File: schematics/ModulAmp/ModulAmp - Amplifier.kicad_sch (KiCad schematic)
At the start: 0 parts

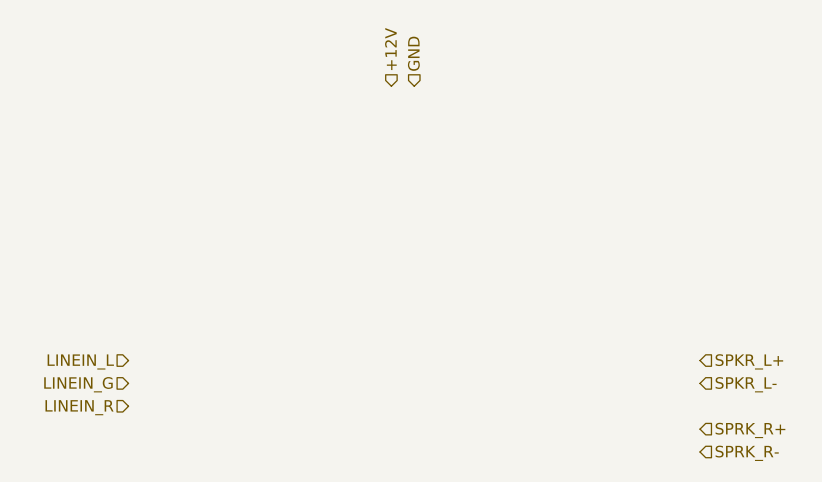
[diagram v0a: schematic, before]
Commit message: Refactored strings and added DHTxx full support
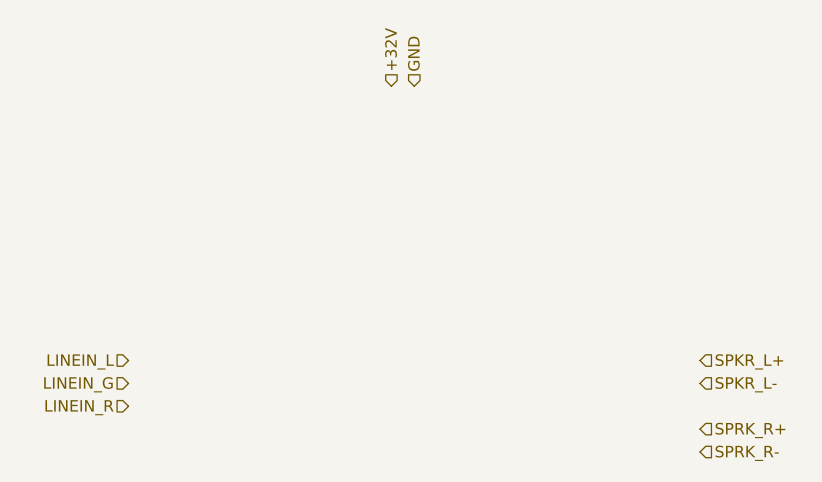
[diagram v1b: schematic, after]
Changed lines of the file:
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@@
     (effects (font (size 1.27 1.27)) (justify left))
   )
-  (hierarchical_label "+12V" (shape input) (at 139.7 43.18 90)
+  (hierarchical_label "+32V" (shape input) (at 139.7 43.18 90)
     (effects (font (size 1.27 1.27)) (justify left))
   )
